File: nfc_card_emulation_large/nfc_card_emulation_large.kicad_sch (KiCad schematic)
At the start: 4 parts, among them J1 Qwiic

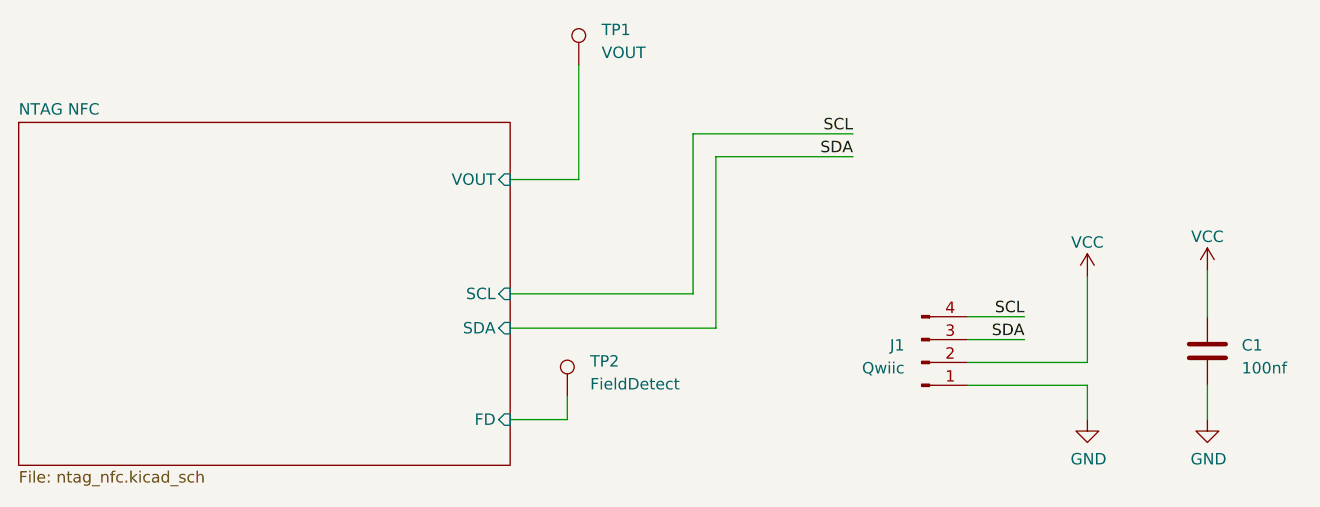
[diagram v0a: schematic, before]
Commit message: Added front artwork to nfc_card_emulation_large
Also created BOM and pos files
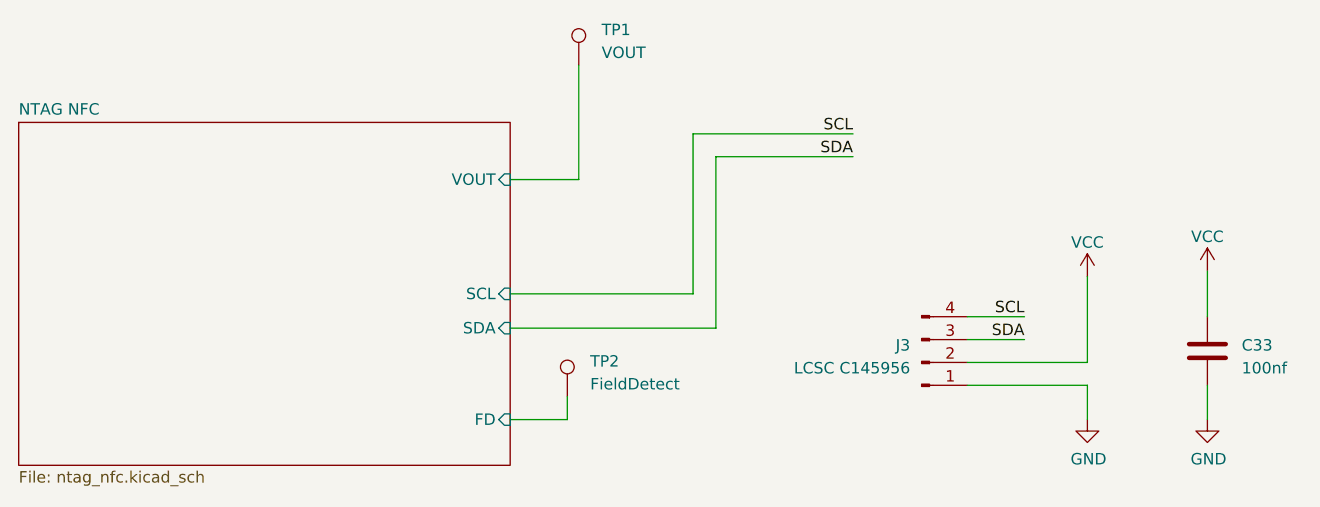
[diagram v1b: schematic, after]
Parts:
- J3: renamed from J1; value Qwiic -> LCSC C145956
- TP1, TP2: now left out of the parts list
- renumbered C1 to C33
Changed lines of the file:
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@@
   (title_block
     (title "NFC Card Emulation only")
-    (date "2023-05-07")
-    (rev "1.0")
+    (date "2023-06-22")
+    (rev "1.1")
     (comment 1 "CC-BY-SA")
   )
@@
   )
   (symbol (lib_id "Connector:TestPoint") (at 92.71 118.11 0) (unit 1)
-    (in_bom yes) (on_board yes) (dnp no) (fields_autoplaced)
+    (in_bom no) (on_board yes) (dnp no) (fields_autoplaced)
     (property "Reference" "TP2" (at 95.25 114.173 0)
       (effects (font (size 1.27 1.27)) (justify left))
@@
     (pin "1")
     (instances
-      (project "nfc_card_emulation"
+      (project "nfc_card_emulation_large"
         (path "/01149b17-33ef-4823-97dd-2a81938478fb"
           (reference "TP2") (unit 1)
@@
     (pin "1")
     (instances
-      (project "nfc_card_emulation"
+      (project "nfc_card_emulation_large"
         (path "/01149b17-33ef-4823-97dd-2a81938478fb"
           (reference "#PWR04") (unit 1)
@@
     (pin "1")
     (instances
-      (project "nfc_card_emulation"
+      (project "nfc_card_emulation_large"
         (path "/01149b17-33ef-4823-97dd-2a81938478fb"
           (reference "#PWR03") (unit 1)
@@
     (pin "1")
     (instances
-      (project "nfc_card_emulation"
+      (project "nfc_card_emulation_large"
         (path "/01149b17-33ef-4823-97dd-2a81938478fb"
           (reference "#PWR06") (unit 1)
@@
     (pin "1")
     (instances
-      (project "nfc_card_emulation"
+      (project "nfc_card_emulation_large"
         (path "/01149b17-33ef-4823-97dd-2a81938478fb"
           (reference "#PWR05") (unit 1)
@@
   (symbol (lib_id "Device:C") (at 163.83 113.03 0) (unit 1)
     (in_bom yes) (on_board yes) (dnp no) (fields_autoplaced)
-    (property "Reference" "C1" (at 167.64 112.395 0)
+    (property "Reference" "C33" (at 167.64 112.395 0)
       (effects (font (size 1.27 1.27)) (justify left))
     )
@@
     (pin "2")
     (instances
-      (project "nfc_card_emulation"
-        (path "/01149b17-33ef-4823-97dd-2a81938478fb"
-          (reference "C1") (unit 1)
+      (project "nfc_card_emulation_large"
+        (path "/01149b17-33ef-4823-97dd-2a81938478fb"
+          (reference "C33") (unit 1)
         )
       )
@@
   (symbol (lib_id "Connector:Conn_01x04_Male") (at 132.08 114.3 0) (mirror x) (unit 1)
     (in_bom yes) (on_board yes) (dnp no) (fields_autoplaced)
-    (property "Reference" "J1" (at 130.175 112.3949 0)
-      (effects (font (size 1.27 1.27)) (justify right))
-    )
-    (property "Value" "Qwiic" (at 130.175 114.9349 0)
+    (property "Reference" "J3" (at 130.81 112.395 0)
+      (effects (font (size 1.27 1.27)) (justify right))
+    )
+    (property "Value" "LCSC C145956" (at 130.81 114.935 0)
       (effects (font (size 1.27 1.27)) (justify right))
     )
@@
     (pin "4")
     (instances
-      (project "nfc_card_emulation"
-        (path "/01149b17-33ef-4823-97dd-2a81938478fb"
-          (reference "J1") (unit 1)
+      (project "nfc_card_emulation_large"
+        (path "/01149b17-33ef-4823-97dd-2a81938478fb"
+          (reference "J3") (unit 1)
         )
       )
@@
   )
   (symbol (lib_id "Connector:TestPoint") (at 93.98 81.28 0) (unit 1)
-    (in_bom yes) (on_board yes) (dnp no) (fields_autoplaced)
+    (in_bom no) (on_board yes) (dnp no) (fields_autoplaced)
     (property "Reference" "TP1" (at 96.52 77.343 0)
       (effects (font (size 1.27 1.27)) (justify left))
@@
     (pin "1")
     (instances
-      (project "nfc_card_emulation"
+      (project "nfc_card_emulation_large"
         (path "/01149b17-33ef-4823-97dd-2a81938478fb"
           (reference "TP1") (unit 1)
@@
     )
     (instances
-      (project "nfc_card_emulation"
+      (project "nfc_card_emulation_large"
         (path "/01149b17-33ef-4823-97dd-2a81938478fb" (page "4"))
       )
